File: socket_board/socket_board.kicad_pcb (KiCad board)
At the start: 2 copper layers, 114.3 x 36.8 mm, 17 parts, among them J1 Barrel_Jack_Switch, J2 DIN-5_180degree, J3 DIN-5_180degree, J4 AudioJack3, J5 AudioJack3, J6 Conn_01x02_Male, J7 Conn_01x03_Male, J8 Conn_01x05_Male, J9 Conn_01x02_Male, K1 G6K-2

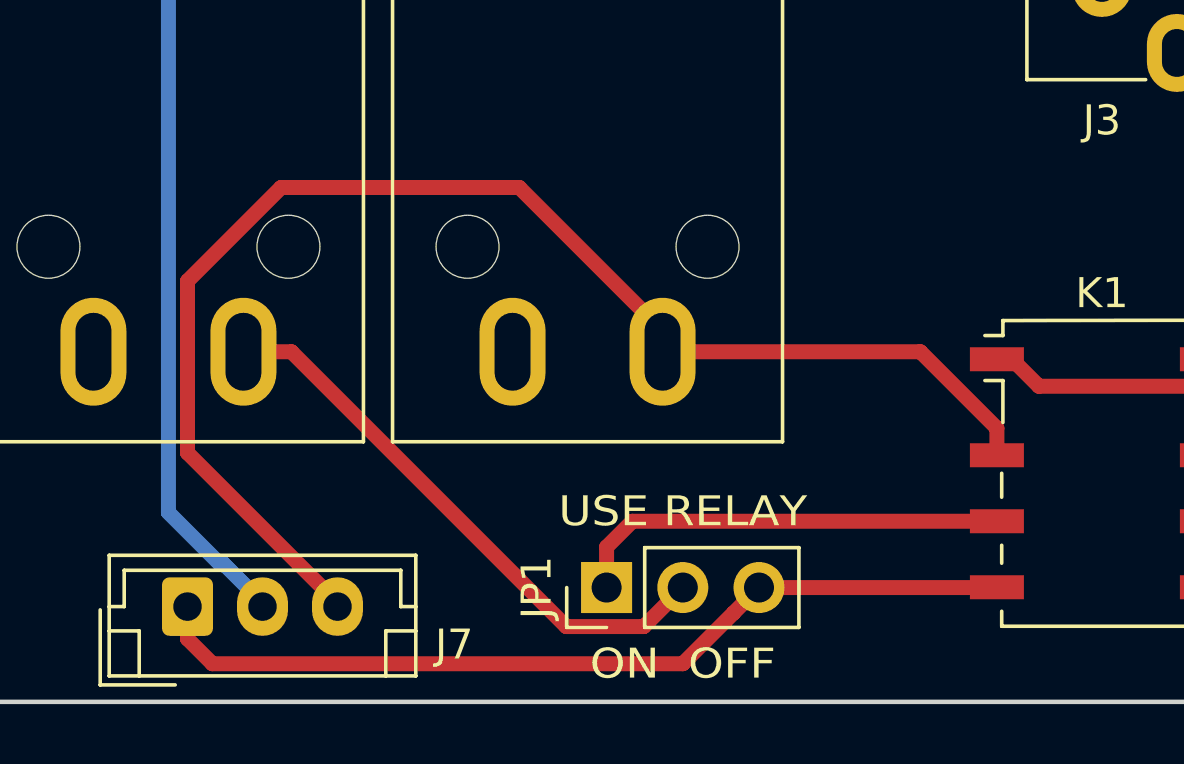
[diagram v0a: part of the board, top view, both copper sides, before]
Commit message: Phone Jack fix
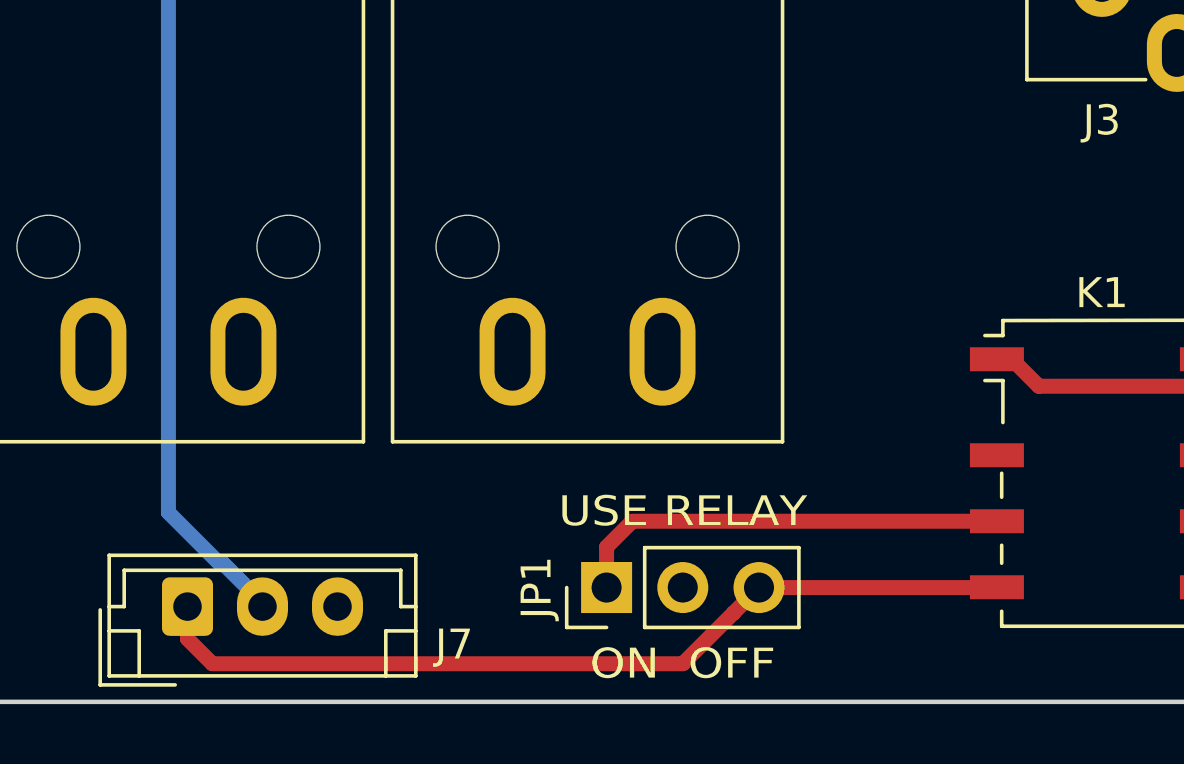
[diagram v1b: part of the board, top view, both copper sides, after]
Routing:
- net IN_T: track 45.8 -> 0.00 mm
- net Net-(J5-PadT): track 19.0 -> 0.00 mm
